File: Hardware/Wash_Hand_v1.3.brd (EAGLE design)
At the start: 71.1 x 48.3 mm, 27 parts, among them J1 I2C, J2 ICSP, J3 SPI, J4 INTERRUPT, J5 EXT_VCC, Q1 16.0 Mhz, U1 328P

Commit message: Hardware: Split out using darnok_[common,led,usb] instead of the single one.
As the darnok_misc is going away.

Signed-off-by: Konrad Rzeszutek Wilk <konrad@darnok.org>
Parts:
- R1, R2, R3, R4, R5, R6, R7, R8, R9: device darnok_misc:RESISTOR -> darnok_common:RESISTOR
- U$4: device darnok_misc:USB_MICROB_10118194_AMPHENOL -> darnok_usb:USB_MICROB_10118194_AMPHENOL
- U$5: device darnok_misc:HDSP-B0XE -> darnok_led:HDSP-B0XE
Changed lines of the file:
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@@
 <attribute name="VALUE" x="38.227" y="10.16" size="1.27" layer="27" ratio="10" rot="R90"/>
 </element>
-<element name="R1" library="darnok_misc" package="RESISTOR" value="220K" x="57.15" y="11.43" smashed="yes" rot="R90">
+<element name="R1" library="darnok_common" package="RESISTOR" value="220K" x="57.15" y="11.43" smashed="yes" rot="R90">
 <attribute name="NAME" x="55.88" y="12.7" size="1.27" layer="25" rot="R90"/>
 <attribute name="VALUE" x="59.69" y="12.7" size="1.27" layer="27" rot="R90"/>
 </element>
-<element name="R2" library="darnok_misc" package="RESISTOR" value="220K" x="3.81" y="20.32" smashed="yes" rot="R90">
+<element name="R2" library="darnok_common" package="RESISTOR" value="220K" x="3.81" y="20.32" smashed="yes" rot="R90">
 <attribute name="NAME" x="2.54" y="21.59" size="1.27" layer="25" rot="R90"/>
 <attribute name="VALUE" x="6.35" y="21.59" size="1.27" layer="27" rot="R90"/>
 </element>
-<element name="R3" library="darnok_misc" package="RESISTOR" value="220K" x="16.51" y="11.43" smashed="yes" rot="R90">
+<element name="R3" library="darnok_common" package="RESISTOR" value="220K" x="16.51" y="11.43" smashed="yes" rot="R90">
 <attribute name="NAME" x="15.24" y="12.7" size="1.27" layer="25" rot="R90"/>
 <attribute name="VALUE" x="19.05" y="12.7" size="1.27" layer="27" rot="R90"/>
 </element>
-<element name="R4" library="darnok_misc" package="RESISTOR" value="220K" x="41.91" y="11.43" smashed="yes" rot="R90">
+<element name="R4" library="darnok_common" package="RESISTOR" value="220K" x="41.91" y="11.43" smashed="yes" rot="R90">
 <attribute name="NAME" x="40.64" y="12.7" size="1.27" layer="25" rot="R90"/>
 <attribute name="VALUE" x="44.45" y="12.7" size="1.27" layer="27" rot="R90"/>
 </element>
-<element name="R5" library="darnok_misc" package="RESISTOR" value="220K" x="46.99" y="11.43" smashed="yes" rot="R90">
+<element name="R5" library="darnok_common" package="RESISTOR" value="220K" x="46.99" y="11.43" smashed="yes" rot="R90">
 <attribute name="NAME" x="45.72" y="12.7" size="1.27" layer="25" rot="R90"/>
 <attribute name="VALUE" x="49.53" y="12.7" size="1.27" layer="27" rot="R90"/>
 </element>
-<element name="R6" library="darnok_misc" package="RESISTOR" value="220K" x="52.07" y="11.43" smashed="yes" rot="R90">
+<element name="R6" library="darnok_common" package="RESISTOR" value="220K" x="52.07" y="11.43" smashed="yes" rot="R90">
 <attribute name="NAME" x="50.8" y="12.7" size="1.27" layer="25" rot="R90"/>
 <attribute name="VALUE" x="54.61" y="12.7" size="1.27" layer="27" rot="R90"/>
 </element>
-<element name="R7" library="darnok_misc" package="RESISTOR" value="220K" x="11.43" y="11.43" smashed="yes" rot="R90">
+<element name="R7" library="darnok_common" package="RESISTOR" value="220K" x="11.43" y="11.43" smashed="yes" rot="R90">
 <attribute name="NAME" x="10.16" y="12.7" size="1.27" layer="25" rot="R90"/>
 <attribute name="VALUE" x="13.97" y="12.7" size="1.27" layer="27" rot="R90"/>
 </element>
-<element name="R8" library="darnok_misc" package="RESISTOR" value="220K" x="21.59" y="11.43" smashed="yes" rot="R90">
+<element name="R8" library="darnok_common" package="RESISTOR" value="220K" x="21.59" y="11.43" smashed="yes" rot="R90">
 <attribute name="NAME" x="20.32" y="12.7" size="1.27" layer="25" rot="R90"/>
 <attribute name="VALUE" x="24.13" y="12.7" size="1.27" layer="27" rot="R90"/>
 </element>
-<element name="R9" library="darnok_misc" package="RESISTOR" value="10K" x="3.81" y="38.1" smashed="yes" rot="R270">
+<element name="R9" library="darnok_common" package="RESISTOR" value="10K" x="3.81" y="38.1" smashed="yes" rot="R270">
 <attribute name="NAME" x="5.08" y="36.83" size="1.27" layer="25" rot="R270"/>
 <attribute name="VALUE" x="1.27" y="36.83" size="1.27" layer="27" rot="R270"/>
 </element>
-<element name="U$4" library="darnok_misc" package="USB_MICROB_10118194_AMPHENOL" value="USB_MICROB_10118194_AMPHENOL" x="1.27" y="12.7" smashed="yes" rot="R270"/>
-<element name="U$5" library="darnok_misc" package="HDSP-B0XE" value="HDSP-B04E" x="33.528" y="31.496" smashed="yes" rot="MR0">
+<element name="U$4" library="darnok_usb" package="USB_MICROB_10118194_AMPHENOL" value="USB_MICROB_10118194_AMPHENOL" x="1.27" y="12.7" smashed="yes" rot="R270"/>
+<element name="U$5" library="darnok_led" package="HDSP-B0XE" value="HDSP-B04E" x="33.528" y="31.496" smashed="yes" rot="MR0">
 <attribute name="HDSP-B04E" value="" x="-5.842" y="21.336" size="1.778" layer="28" rot="MR0" display="off"/>
 </element>

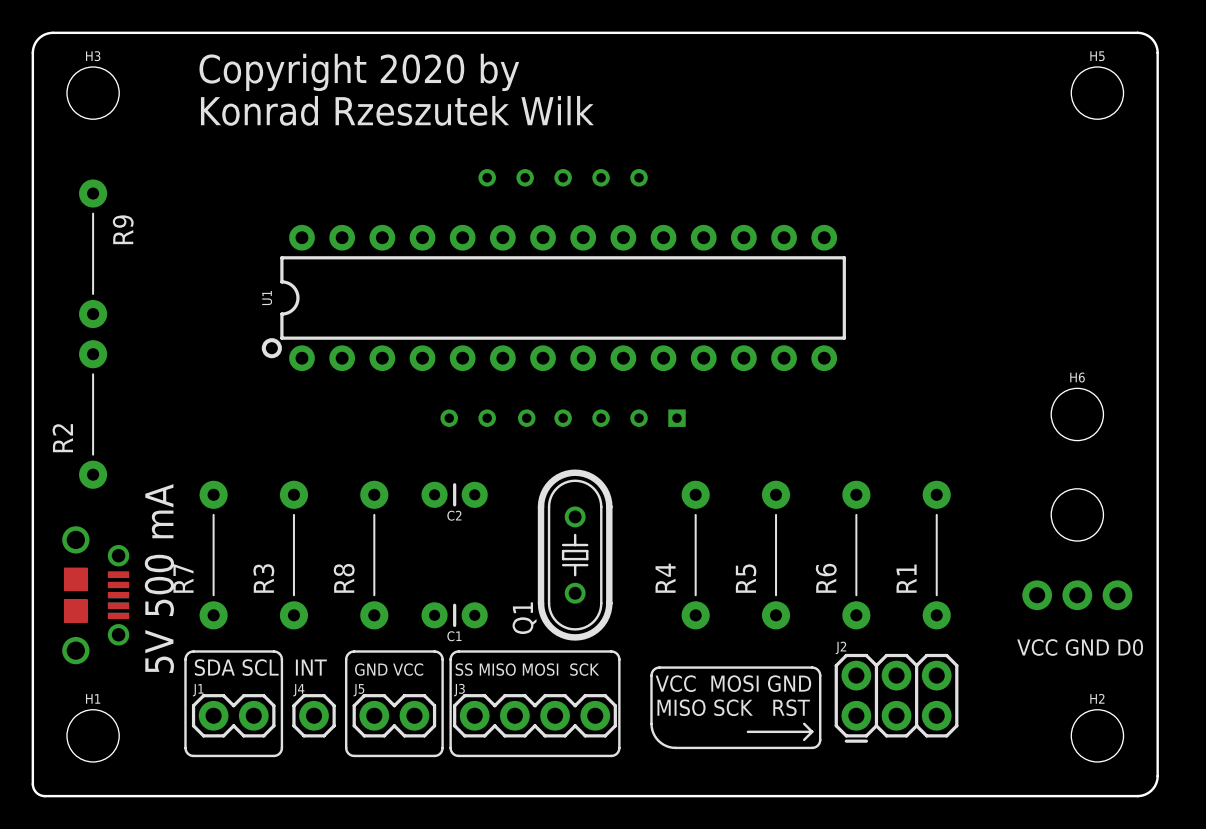
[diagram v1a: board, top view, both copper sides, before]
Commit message: Hardware: Switch to 1206 SMD
Signed-off-by: Konrad Rzeszutek Wilk <konrad@darnok.org>
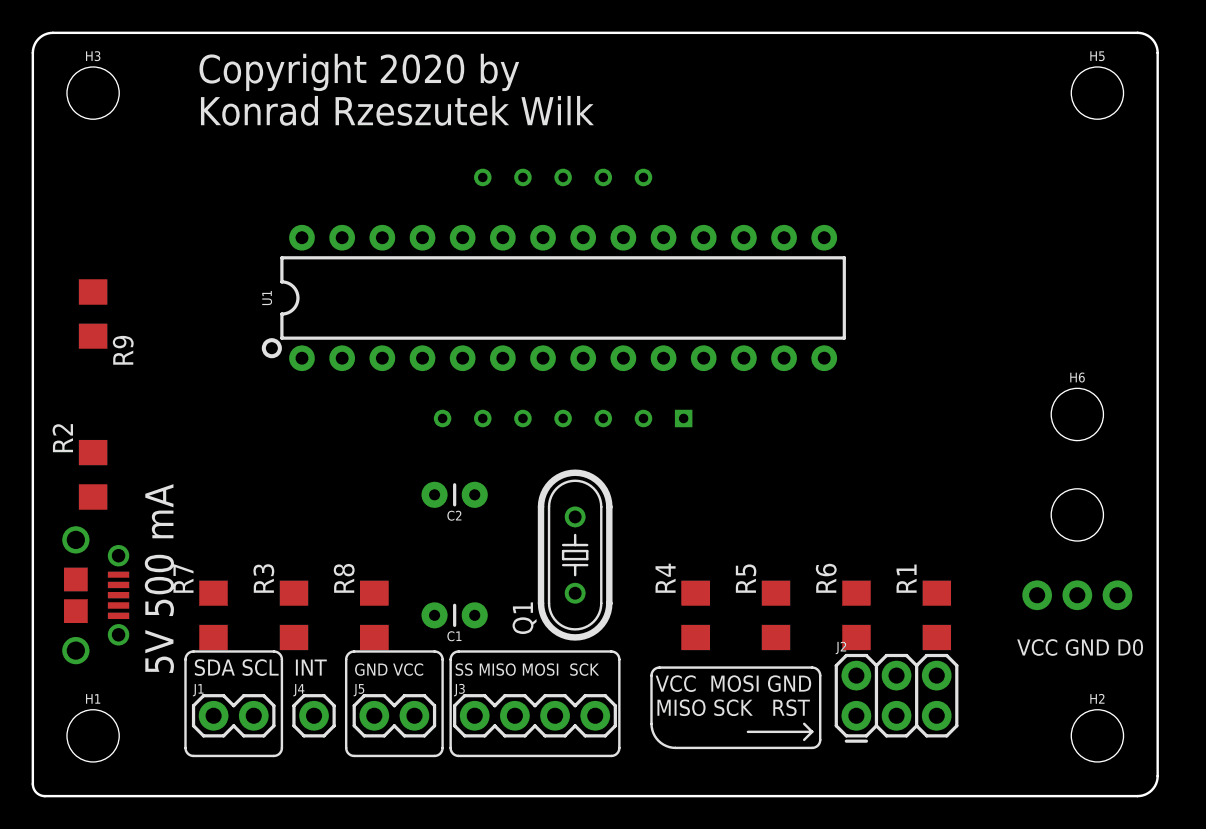
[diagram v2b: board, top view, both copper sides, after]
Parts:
- R1, R2, R3, R4, R5, R6, R7, R8, R9: device darnok_common:RESISTOR -> darnok_common:1206
- moved R9 7.62 mm to (3.81, 30.5)
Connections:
- net A: now also R1.2; no longer R1.R_2
- net B: now also R2.2; no longer R2.R_2
- net C: now also R3.2; no longer R3.R_2
- net D: now also R4.2; no longer R4.R_2
- net DP: now also R8.2; no longer R8.R_2
- net E: now also R5.2; no longer R5.R_2
- net F: now also R6.2; no longer R6.R_2
- net G: now also R7.2; no longer R7.R_2
- net N$1: now also R3.1; no longer R3.R_1
- net N$18: now also R8.1; no longer R8.R_1
- net N$19: now also R6.1; no longer R6.R_1
- net N$2: now also R1.1; no longer R1.R_1
- net N$20: now also R4.1; no longer R4.R_1
- net N$21: now also R2.1; no longer R2.R_1
- net N$3: now also R5.1; no longer R5.R_1
- net N$4: now also R7.1; no longer R7.R_1
- net RESET: now also R9.1; no longer R9.R_1
- net VCC: now also R9.2; no longer R9.R_2

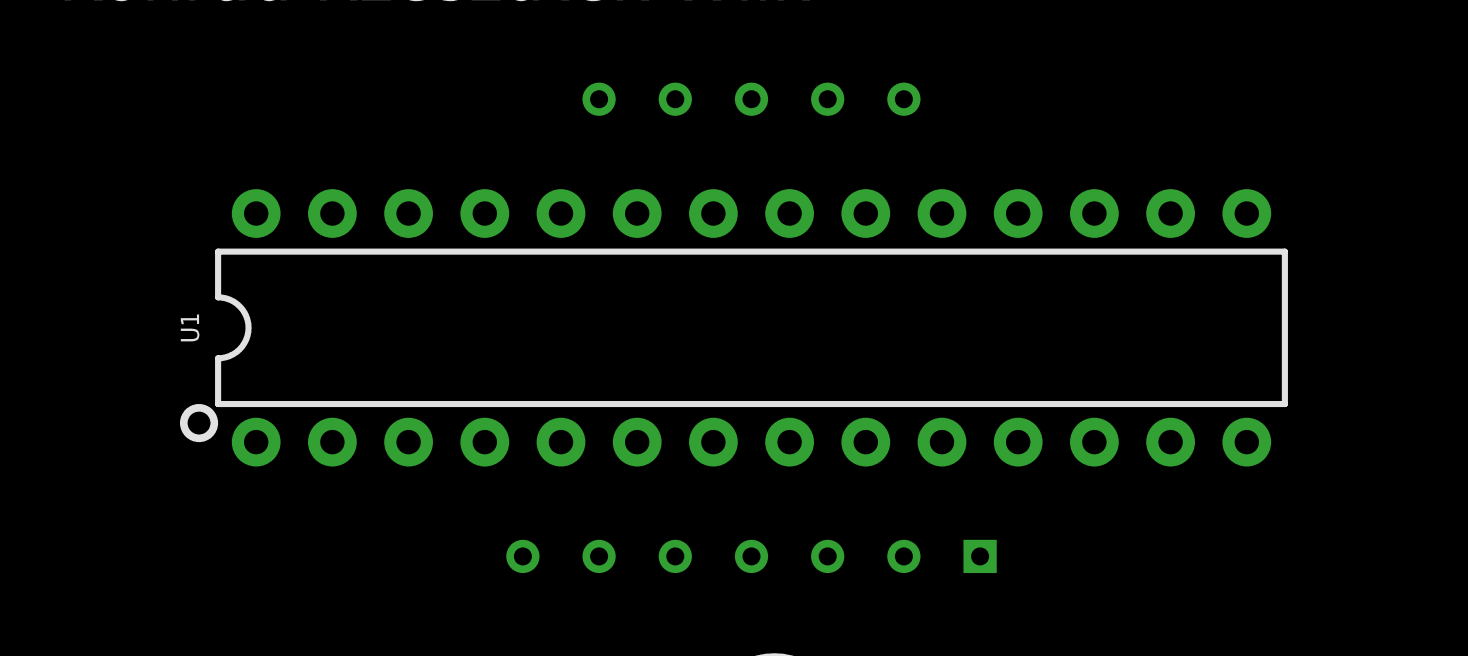
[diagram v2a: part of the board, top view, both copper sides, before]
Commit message: Hardware: Switch to TQFP32 on ATMEGA328P
Signed-off-by: Konrad Rzeszutek Wilk <konrad@darnok.org>
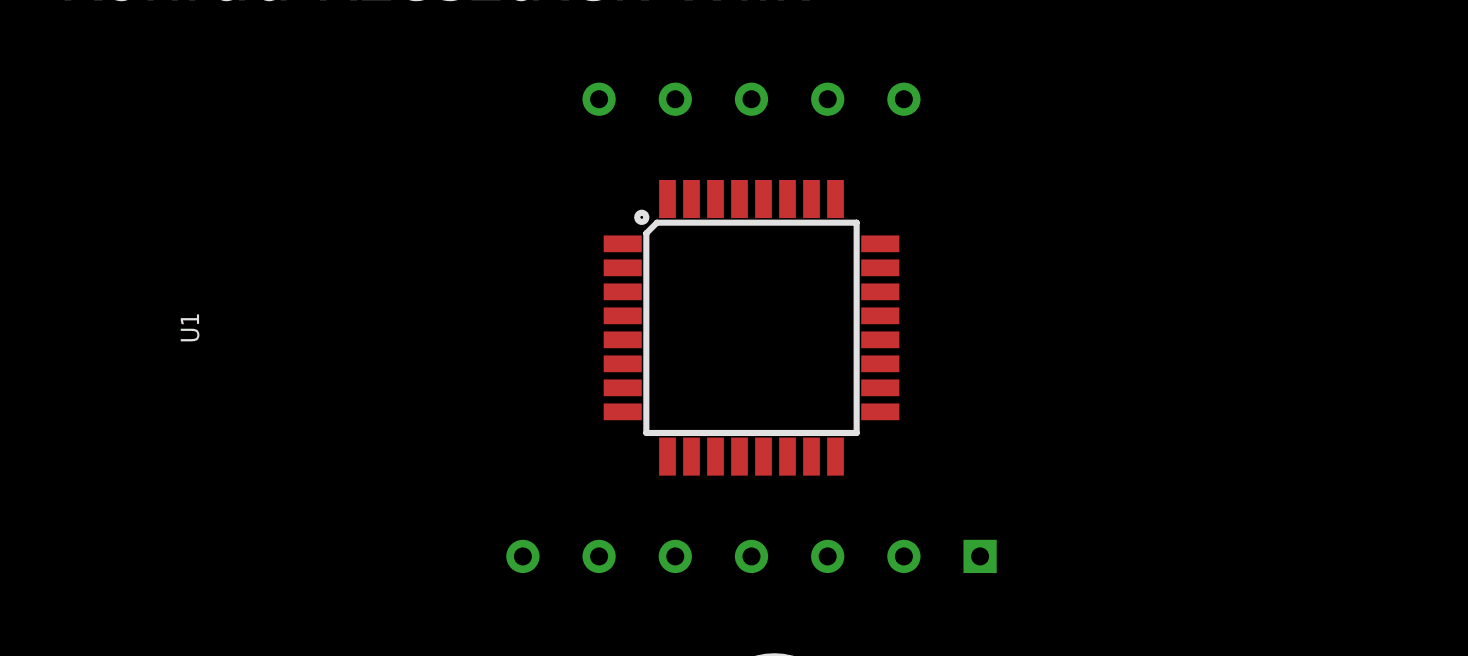
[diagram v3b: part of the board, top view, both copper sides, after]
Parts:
- U1: value 328P -> ATMEGA328P_TQFP; device SparkFun-IC-Microcontroller:DIP28 -> SparkFun-IC-Microcontroller:TQFP32-08
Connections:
- net 0: now also U1.21, U1.3, U1.5; no longer U1.22, U1.8
- net D1: now also U1.12; no longer U1.14
- net INTERRUPT: now also U1.32; no longer U1.4
- net MISO: now also U1.16; no longer U1.18
- net MOSI: now also U1.15; no longer U1.17
- net N$1: now also U1.13; no longer U1.15
- net N$18: now also U1.11; no longer U1.13
- net N$19: now also U1.9; no longer U1.11
- net N$2: now also U1.30; no longer U1.2
- net N$20: now also U1.1; no longer U1.5
- net N$21: now also U1.31; no longer U1.3
- net N$3: now also U1.2; no longer U1.6
- net N$4: now also U1.10; no longer U1.12
- net N$8: now also U1.8; no longer U1.10
- net N$9: now also U1.7; no longer U1.9
- net RESET: now also U1.29; no longer U1.1
- net SCK: now also U1.17; no longer U1.19
- net SS: now also U1.14; no longer U1.16
- net VCC: now also U1.18, U1.4, U1.6; no longer U1.21, U1.7

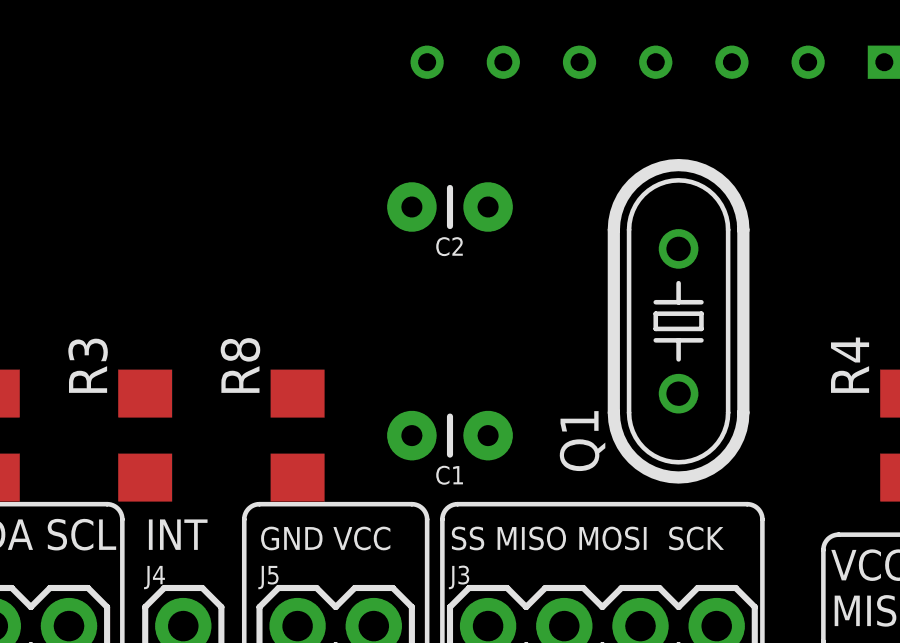
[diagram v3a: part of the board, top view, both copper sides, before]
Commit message: Hardware: Switch capacitor to 1206 SMD
Signed-off-by: Konrad Rzeszutek Wilk <konrad@darnok.org>
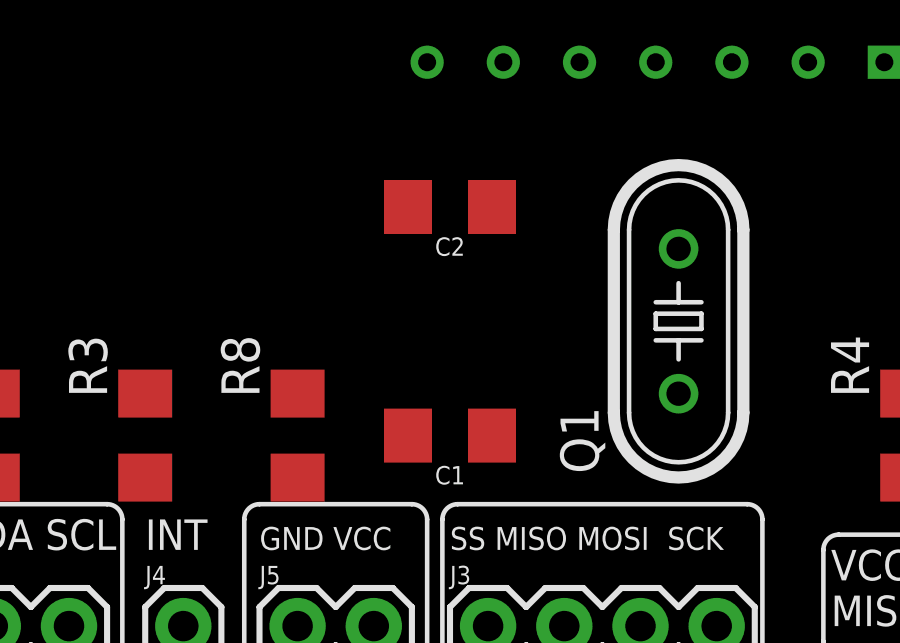
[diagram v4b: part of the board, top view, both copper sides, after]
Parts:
- C1, C2: device SparkFun-Capacitors:CAP-PTH-2.54 -> SparkFun-Capacitors:1206
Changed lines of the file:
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@@
 </autorouter>
 <elements>
-<element name="C1" library="SparkFun-Capacitors" library_urn="urn:adsk.eagle:library:510" package="CAP-PTH-2.54" package3d_urn="urn:adsk.eagle:package:37435/1" value="22pF" x="26.67" y="11.43" smashed="yes" rot="R180">
+<element name="C1" library="SparkFun-Capacitors" library_urn="urn:adsk.eagle:library:510" package="1206" package3d_urn="urn:adsk.eagle:package:37426/1" value="22pF" x="26.67" y="11.43" smashed="yes" rot="R180">
 <attribute name="NAME" x="26.67" y="10.414" size="0.6096" layer="25" font="vector" ratio="20" rot="R180" align="bottom-center"/>
-<attribute name="PROD_ID" value="CAP-09128" x="3.81" y="66.04" size="1.778" layer="27" rot="R180" display="off"/>
-<attribute name="VALUE" x="26.67" y="12.446" size="0.6096" layer="27" font="vector" ratio="20" rot="R180" align="top-center"/>
+<attribute name="PROD_ID" value="CAP-10057" x="3.81" y="66.04" size="1.778" layer="27" rot="R180" display="off"/>
+<attribute name="VALUE" value="10uF" x="26.67" y="12.446" size="0.6096" layer="27" font="vector" ratio="20" rot="R180" align="top-center"/>
 </element>
-<element name="C2" library="SparkFun-Capacitors" library_urn="urn:adsk.eagle:library:510" package="CAP-PTH-2.54" package3d_urn="urn:adsk.eagle:package:37435/1" value="22pF" x="26.67" y="19.05" smashed="yes" rot="R180">
+<element name="C2" library="SparkFun-Capacitors" library_urn="urn:adsk.eagle:library:510" package="1206" package3d_urn="urn:adsk.eagle:package:37426/1" value="22pF" x="26.67" y="19.05" smashed="yes" rot="R180">
 <attribute name="NAME" x="26.67" y="18.034" size="0.6096" layer="25" font="vector" ratio="20" rot="R180" align="bottom-center"/>
-<attribute name="PROD_ID" value="CAP-09128" x="-1.27" y="73.66" size="1.778" layer="27" rot="R180" display="off"/>
-<attribute name="VALUE" x="26.67" y="20.066" size="0.6096" layer="27" font="vector" ratio="20" rot="R180" align="top-center"/>
+<attribute name="PROD_ID" value="CAP-10057" x="-1.27" y="73.66" size="1.778" layer="27" rot="R180" display="off"/>
+<attribute name="VALUE" value="10uF" x="26.67" y="20.066" size="0.6096" layer="27" font="vector" ratio="20" rot="R180" align="top-center"/>
 </element>
 <element name="J" library="SparkFun-Connectors" library_urn="urn:adsk.eagle:library:513" package="1X03" package3d_urn="urn:adsk.eagle:package:38063/1" value="D0    GND  VCC  ," x="63.5" y="12.7" smashed="yes" rot="MR180">
@@
 <contactref element="U1" pad="5"/>
 <wire x1="57.15" y1="7.62" x2="66.04" y2="12.7" width="0" layer="19" extent="1-1"/>
-<wire x1="27.94" y1="11.43" x2="57.15" y2="7.62" width="0" layer="19" extent="1-1"/>
-<wire x1="27.94" y1="19.05" x2="27.94" y2="11.43" width="0" layer="19" extent="1-1"/>
-<wire x1="21.59" y1="5.08" x2="27.94" y2="11.43" width="0" layer="19" extent="1-1"/>
-<wire x1="29.2354" y1="31.096" x2="27.94" y2="19.05" width="0" layer="19" extent="1-1"/>
+<wire x1="28.07" y1="11.43" x2="57.15" y2="7.62" width="0" layer="19" extent="1-1"/>
+<wire x1="28.07" y1="19.05" x2="28.07" y2="11.43" width="0" layer="19" extent="1-1"/>
+<wire x1="21.59" y1="5.08" x2="28.07" y2="11.43" width="0" layer="19" extent="1-1"/>
+<wire x1="29.2354" y1="31.096" x2="28.07" y2="19.05" width="0" layer="19" extent="1-1"/>
 <wire x1="29.2354" y1="32.696" x2="29.2354" y2="31.096" width="0" layer="19" extent="1-1"/>
 <wire x1="37.8206" y1="31.896" x2="29.2354" y2="31.096" width="0" layer="19" extent="1-1"/>
@@
 <contactref element="U1" pad="8"/>
 <wire x1="34.29" y1="17.653" x2="29.2354" y2="28.696" width="0" layer="19" extent="1-1"/>
-<wire x1="25.4" y1="11.43" x2="34.29" y2="17.653" width="0" layer="19" extent="1-1"/>
+<wire x1="25.27" y1="11.43" x2="34.29" y2="17.653" width="0" layer="19" extent="1-1"/>
 </signal>
 <signal name="N$9">
@@
 <contactref element="U1" pad="7"/>
 <contactref element="C2" pad="2"/>
-<wire x1="25.4" y1="19.05" x2="29.2354" y2="29.496" width="0" layer="19" extent="1-1"/>
-<wire x1="34.29" y1="12.827" x2="25.4" y2="19.05" width="0" layer="19" extent="1-1"/>
+<wire x1="25.27" y1="19.05" x2="29.2354" y2="29.496" width="0" layer="19" extent="1-1"/>
+<wire x1="34.29" y1="12.827" x2="25.27" y2="19.05" width="0" layer="19" extent="1-1"/>
 </signal>
 <signal name="D0">
